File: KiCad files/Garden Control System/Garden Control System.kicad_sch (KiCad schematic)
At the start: 0 parts

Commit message: expanded power supply section. completed LSD design. sized shunt resistors
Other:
- sheet Sensors and HSDs renamed LSD and Current Sense
- note added: "Analog Input"
- note added: "Communication"
- note added: "DI/O"
- note added: "DISPLAY, SENSORS?"
- note added: "Display"
- note added: "GATE DRIVERS"
- note added: "Legend"
- note added: "MICRO, PHY,"
- note added: "PUMPS/FANS"
- note added: "PWM"

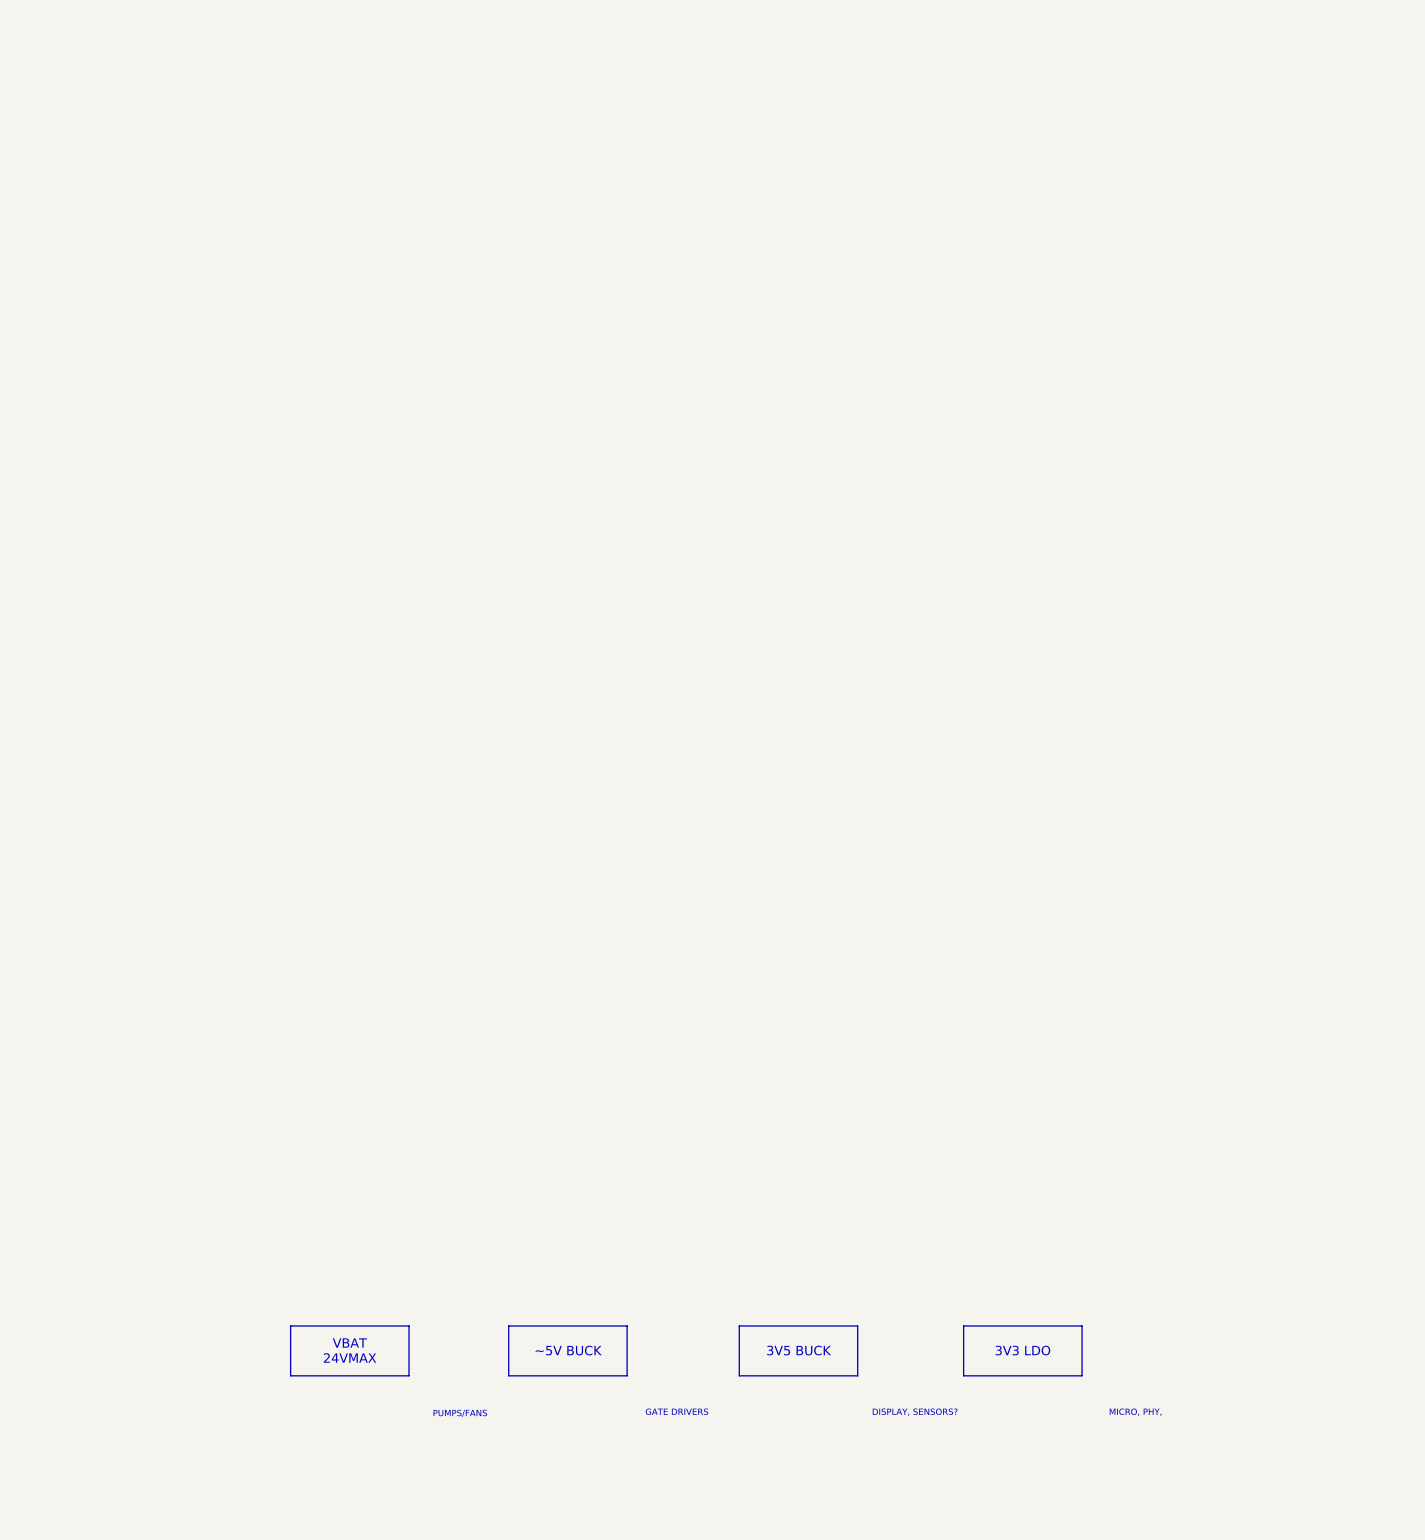
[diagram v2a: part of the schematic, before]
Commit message: adding recent schematic progress
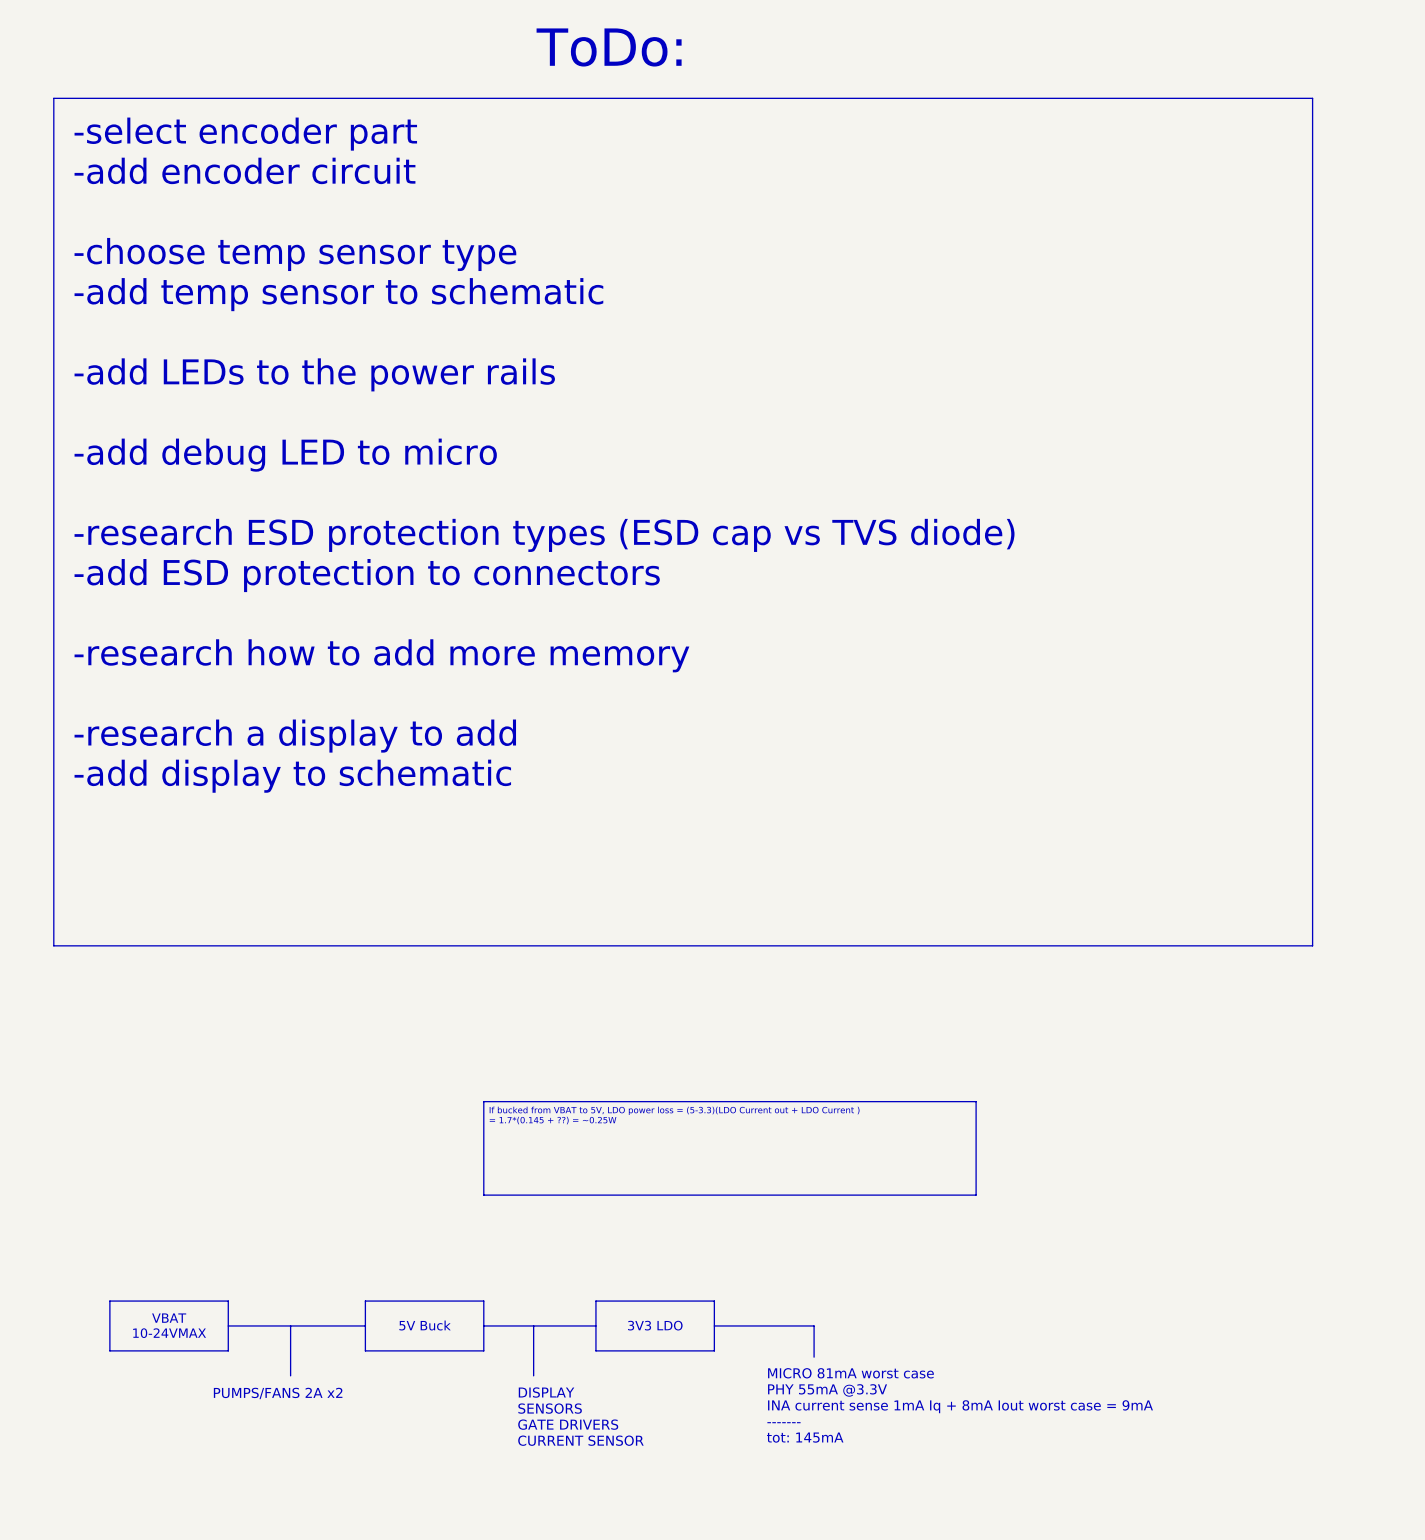
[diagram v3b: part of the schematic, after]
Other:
- note added: "DISPLAY SENSORS GATE DRIVERS CURRENT SENSOR"
- note added: "MICRO 81mA worst case PHY 55mA @3.3V INA current sense 1mA Iq + 8mA Iout worst case = 9mA ------- tot: 145mA"
- note added: "PUMPS/FANS 2A x2"
- note added: "ToDo:"
- note removed: "DISPLAY, SENSORS?"
- note removed: "GATE DRIVERS"
- note removed: "MICRO, PHY,"
- note removed: "PUMPS/FANS"
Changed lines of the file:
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@@
 		(company "Lee Evans")
+	)
+	(polyline
+		(pts
+			(xy 105.41 31.75) (xy 128.27 31.75)
+		)
+		(stroke
+			(width 0)
+			(type default)
+		)
+	)
+	(polyline
+		(pts
+			(xy 53.34 31.75) (xy 81.28 31.75)
+		)
+		(stroke
+			(width 0)
+			(type default)
+		)
+	)
+	(polyline
+		(pts
+			(xy 115.57 31.75) (xy 115.57 41.91)
+		)
+		(stroke
+			(width 0)
+			(type default)
+		)
+	)
+	(polyline
+		(pts
+			(xy 152.4 31.75) (xy 172.72 31.75)
+		)
+		(stroke
+			(width 0)
+			(type default)
+		)
+	)
+	(polyline
+		(pts
+			(xy 66.04 31.75) (xy 66.04 41.91)
+		)
+		(stroke
+			(width 0)
+			(type default)
+		)
+	)
+	(polyline
+		(pts
+			(xy 172.72 31.75) (xy 172.72 38.1)
+		)
+		(stroke
+			(width 0)
+			(type default)
+		)
 	)
 	(rectangle
@@
 		(fill
 			(type color)
-			(color 255 255 194 1)
+			(color 72 72 72 1)
+		)
+	)
+	(text_box "If bucked from VBAT to 5V, LDO power loss = (5-3.3)(LDO Current out + LDO Current ) \n= 1.7*(0.145 + ??) = ~0.25W"
+		(exclude_from_sim no)
+		(at 105.41 -13.97 0)
+		(size 100.33 19.05)
+		(stroke
+			(width 0)
+			(type default)
+		)
+		(fill
+			(type none)
+		)
+		(effects
+			(font
+				(size 1.27 1.27)
+			)
+			(justify left top)
 		)
 	)
 	(text_box "3V3 LDO"
 		(exclude_from_sim no)
-		(at 203.2 31.75 0)
+		(at 128.27 26.67 0)
 		(size 24.13 10.16)
 		(stroke
@@
 		)
 		(fill
+			(type color)
+			(color 0 0 132 0.34)
+		)
+		(effects
+			(font
+				(size 1.905 1.905)
+				(color 255 255 255 1)
+			)
+		)
+	)
+	(text_box "-select encoder part\n-add encoder circuit\n\n-choose temp sensor type\n-add temp sensor to schematic\n\n-add LEDs to the power rails\n\n-add debug LED to micro\n\n-research ESD protection types (ESD cap vs TVS diode)\n-add ESD protection to connectors\n\n-research how to add more memory\n\n-research a display to add\n-add display to schematic\n\n"
+		(exclude_from_sim no)
+		(at 17.78 -218.44 0)
+		(size 256.54 172.72)
+		(stroke
+			(width 0)
+			(type default)
+		)
+		(fill
 			(type none)
 		)
 		(effects
 			(font
+				(size 5.08 5.08)
+			)
+			(justify left top)
+		)
+	)
+	(text_box "5V Buck"
+		(exclude_from_sim no)
+		(at 81.28 26.67 0)
+		(size 24.13 10.16)
+		(stroke
+			(width 0)
+			(type default)
+		)
+		(fill
+			(type color)
+			(color 0 0 132 0.68)
+		)
+		(effects
+			(font
 				(size 1.905 1.905)
-			)
-		)
-	)
-	(text_box "3V5 BUCK"
-		(exclude_from_sim no)
-		(at 157.48 31.75 0)
-		(size 24.13 10.16)
-		(stroke
-			(width 0)
-			(type default)
-		)
-		(fill
-			(type none)
-		)
-		(effects
-			(font
-				(size 1.905 1.905)
+				(color 255 255 255 1)
 			)
 		)
@@
 			(font
 				(size 2.032 2.032)
-			)
-		)
-	)
-	(text_box "~5V BUCK"
-		(exclude_from_sim no)
-		(at 110.49 31.75 0)
-		(size 24.13 10.16)
-		(stroke
-			(width 0)
-			(type default)
-		)
-		(fill
-			(type none)
-		)
-		(effects
-			(font
-				(size 1.905 1.905)
 			)
 		)
@@
 		)
 	)
-	(text_box "VBAT\n24VMAX"
-		(exclude_from_sim no)
-		(at 66.04 31.75 0)
+	(text_box "VBAT\n10-24VMAX"
+		(exclude_from_sim no)
+		(at 29.21 26.67 0)
 		(size 24.13 10.16)
 		(stroke
@@
 		)
 		(fill
-			(type none)
+			(type color)
+			(color 0 0 132 1)
 		)
 		(effects
 			(font
 				(size 1.905 1.905)
+				(color 255 255 255 1)
 			)
 		)
@@
 		)
 	)
-	(text "PUMPS/FANS"
-		(exclude_from_sim no)
-		(at 100.584 49.784 0)
-		(effects
-			(font
-				(size 1.27 1.27)
-			)
-		)
-	)
-	(text "GATE DRIVERS"
-		(exclude_from_sim no)
-		(at 144.78 49.53 0)
-		(effects
-			(font
-				(size 1.27 1.27)
+	(text "PUMPS/FANS 2A x2 "
+		(exclude_from_sim no)
+		(at 63.5 45.72 0)
+		(effects
+			(font
+				(size 2.032 2.032)
 			)
 		)
@@
 		)
 	)
-	(text "MICRO, PHY, "
-		(exclude_from_sim no)
-		(at 238.252 49.53 0)
-		(effects
-			(font
-				(size 1.27 1.27)
-			)
+	(text "MICRO 81mA worst case\nPHY 55mA @3.3V\nINA current sense 1mA Iq + 8mA Iout worst case = 9mA\n-------\ntot: 145mA"
+		(exclude_from_sim no)
+		(at 163.068 48.26 0)
+		(effects
+			(font
+				(size 2.032 2.032)
+			)
+			(justify left)
 		)
 	)
@@
 		)
 	)
-	(text "DISPLAY, SENSORS?"
-		(exclude_from_sim no)
-		(at 193.294 49.53 0)
-		(effects
-			(font
-				(size 1.27 1.27)
-			)
-		)
+	(text "DISPLAY\nSENSORS\nGATE DRIVERS\nCURRENT SENSOR"
+		(exclude_from_sim no)
+		(at 112.268 50.546 0)
+		(effects
+			(font
+				(size 2.032 2.032)
+			)
+			(justify left)
+		)
+	)
+	(text "ToDo:"
+		(exclude_from_sim no)
+		(at 131.572 -228.346 0)
+		(effects
+			(font
+				(size 7.62 7.62)
+				(color 255 0 0 1)
+			)
+		)

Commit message: working on temp sensor circuit
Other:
- added sheet Encoder and Display (Encoder and Display.kicad_sch)
- added sheet Temperature Sensors (Temperature Sensors.kicad_sch)
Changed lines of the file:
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@@
 		)
 	)
-	(text_box "-select encoder part\n-add encoder circuit\n\n-choose temp sensor type\n-add temp sensor to schematic\n\n-add LEDs to the power rails\n\n-add debug LED to micro\n\n-research ESD protection types (ESD cap vs TVS diode)\n-add ESD protection to connectors\n\n-research how to add more memory\n\n-research a display to add\n-add display to schematic\n\n"
+	(text_box "-choose temp sensor type\n-add temp sensor to schematic\n\n-research ESD protection types (ESD cap vs TVS diode)\n-add ESD protection to connectors\n\n-research how to add more memory\n\n-research a display to add\n-add display to schematic\n\n"
 		(exclude_from_sim no)
 		(at 17.78 -218.44 0)
@@
 			)
 			(justify left)
+		)
+	)
+	(sheet
+		(at 7.62 441.96)
+		(size 314.96 181.61)
+		(fields_autoplaced yes)
+		(stroke
+			(width 0.1524)
+			(type solid)
+		)
+		(fill
+			(color 0 0 0 0.0000)
+		)
+		(property "Sheetname" "Encoder and Display"
+			(at 7.62 441.2484 0)
+			(effects
+				(font
+					(size 1.27 1.27)
+				)
+				(justify left bottom)
+			)
+		)
+		(property "Sheetfile" "Encoder and Display.kicad_sch"
+			(at 7.62 624.1546 0)
+			(effects
+				(font
+					(size 1.27 1.27)
+				)
+				(justify left top)
+			)
+		)
+		(instances
+			(project "Garden Control System"
+				(path "/be495e14-3da3-4129-8396-1871cb6cba29"
+					(page "7")
+				)
+			)
 		)
 	)
@@
 				)
 			)
+		)
+	)
+	(sheet
+		(at 335.28 443.23)
+		(size 391.16 182.88)
+		(fields_autoplaced yes)
+		(stroke
+			(width 0.1524)
+			(type solid)
+		)
+		(fill
+			(color 0 0 0 0.0000)
+		)
+		(property "Sheetname" "Temperature Sensors"
+			(at 335.28 442.5184 0)
+			(effects
+				(font
+					(size 1.27 1.27)
+				)
+				(justify left bottom)
+			)
+		)
+		(property "Sheetfile" "Temperature Sensors.kicad_sch"
+			(at 335.28 626.6946 0)
+			(effects
+				(font
+					(size 1.27 1.27)
+				)
+				(justify left top)
+			)
+		)
+		(instances
+			(project "Garden Control System"
+				(path "/be495e14-3da3-4129-8396-1871cb6cba29"
+					(page "8")
+				)
+			)

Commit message: we cookin' again. Added LSD and start temp sense section.
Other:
- sheet LSD and Current Sense renamed Motor Drivers
- added sheet Current Sense (untitled.kicad_sch)
- added sheet pH Sensor (pH Sensor.kicad_sch)
- sheet Motor Drivers: file Sensors and HSDs.kicad_sch -> Motor Drivers.kicad_sch
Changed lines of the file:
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@@
 		)
 	)
-	(text_box "-choose temp sensor type\n-add temp sensor to schematic\n\n-research ESD protection types (ESD cap vs TVS diode)\n-add ESD protection to connectors\n\n-research how to add more memory\n\n-research a display to add\n-add display to schematic\n\n"
+	(text_box "-add temp sensor circuit to schematic\n-add details on encoder operation and connect to micro \n-add pH sensing circuit and info\n-finish eth page\n-\n\n-research ESD protection types (ESD cap vs TVS diode)\n-add ESD protection to connectors\n\n-research a display to add\n-add display to schematic\n\n"
 		(exclude_from_sim no)
 		(at 17.78 -218.44 0)
@@
 			(project "Garden Control System"
 				(path "/be495e14-3da3-4129-8396-1871cb6cba29"
-					(page "7")
+					(page "8")
 				)
 			)
@@
 			(project "Garden Control System"
 				(path "/be495e14-3da3-4129-8396-1871cb6cba29"
-					(page "4")
+					(page "10")
 				)
 			)
@@
 			(project "Garden Control System"
 				(path "/be495e14-3da3-4129-8396-1871cb6cba29"
-					(page "6")
+					(page "9")
 				)
 			)
@@
 	)
 	(sheet
+		(at 746.76 444.5)
+		(size 327.66 180.34)
+		(fields_autoplaced yes)
+		(stroke
+			(width 0.1524)
+			(type solid)
+		)
+		(fill
+			(color 0 0 0 0.0000)
+		)
+		(property "Sheetname" "Current Sense"
+			(at 746.76 443.7884 0)
+			(effects
+				(font
+					(size 1.27 1.27)
+				)
+				(justify left bottom)
+			)
+		)
+		(property "Sheetfile" "untitled.kicad_sch"
+			(at 746.76 625.4246 0)
+			(effects
+				(font
+					(size 1.27 1.27)
+				)
+				(justify left top)
+			)
+		)
+		(instances
+			(project "Garden Control System"
+				(path "/be495e14-3da3-4129-8396-1871cb6cba29"
+					(page "4")
+				)
+			)
+		)
+	)
+	(sheet
 		(at 330.2 -3.81)
 		(size 391.16 201.93)
@@
 	)
 	(sheet
+		(at 7.62 642.62)
+		(size 317.5 165.1)
+		(fields_autoplaced yes)
+		(stroke
+			(width 0.1524)
+			(type solid)
+		)
+		(fill
+			(color 0 0 0 0.0000)
+		)
+		(property "Sheetname" "pH Sensor"
+			(at 7.62 641.9084 0)
+			(effects
+				(font
+					(size 1.27 1.27)
+				)
+				(justify left bottom)
+			)
+		)
+		(property "Sheetfile" "pH Sensor.kicad_sch"
+			(at 7.62 808.3046 0)
+			(effects
+				(font
+					(size 1.27 1.27)
+				)
+				(justify left top)
+			)
+		)
+		(instances
+			(project "Garden Control System"
+				(path "/be495e14-3da3-4129-8396-1871cb6cba29"
+					(page "7")
+				)
+			)
+		)
+	)
+	(sheet
 		(at 746.76 224.79)
 		(size 325.12 198.12)
@@
 			(color 0 0 0 0.0000)
 		)
-		(property "Sheetname" "LSD and Current Sense"
+		(property "Sheetname" "Motor Drivers"
 			(at 746.76 224.0784 0)
 			(effects
@@
 			)
 		)
-		(property "Sheetfile" "Sensors and HSDs.kicad_sch"
+		(property "Sheetfile" "Motor Drivers.kicad_sch"
 			(at 746.76 423.4946 0)
 			(effects
@@
 			(project "Garden Control System"
 				(path "/be495e14-3da3-4129-8396-1871cb6cba29"
-					(page "8")
-				)
-			)
+					(page "6")
+				)
+			)
